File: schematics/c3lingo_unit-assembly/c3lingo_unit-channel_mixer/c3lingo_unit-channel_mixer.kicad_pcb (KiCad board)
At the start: 2 copper layers, 75 x 90 mm, 103 parts, among them J301 Interconnect, J303 I/O, Q301 MMBFJ113, SW301 OnAir_X, SW302 Mute_X, U301 TL072, U302 LM339, U303 LM339, U304 LM339, U305 LM833-N

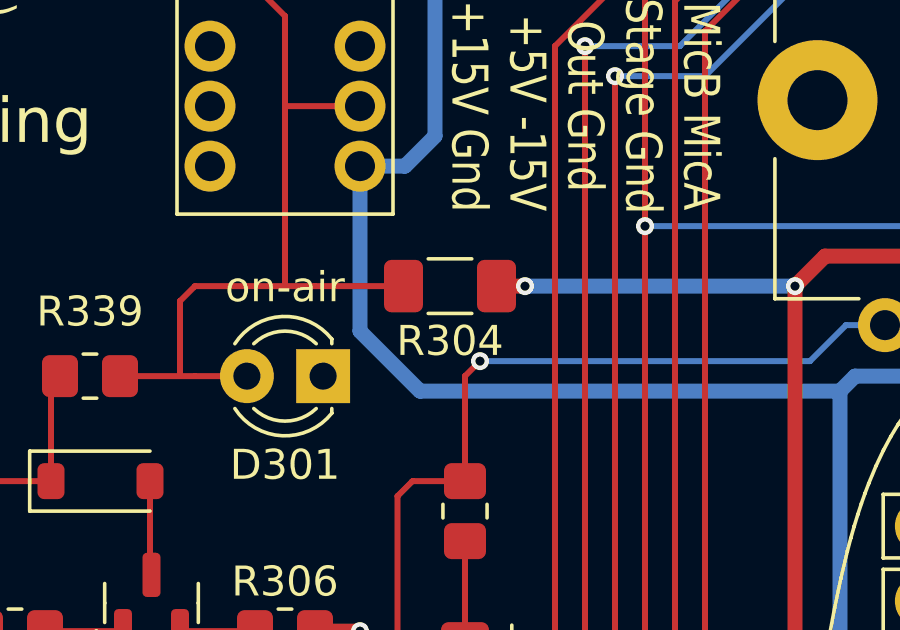
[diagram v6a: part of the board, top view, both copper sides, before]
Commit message: Channel-Mixer: Fix on-air LED resistor
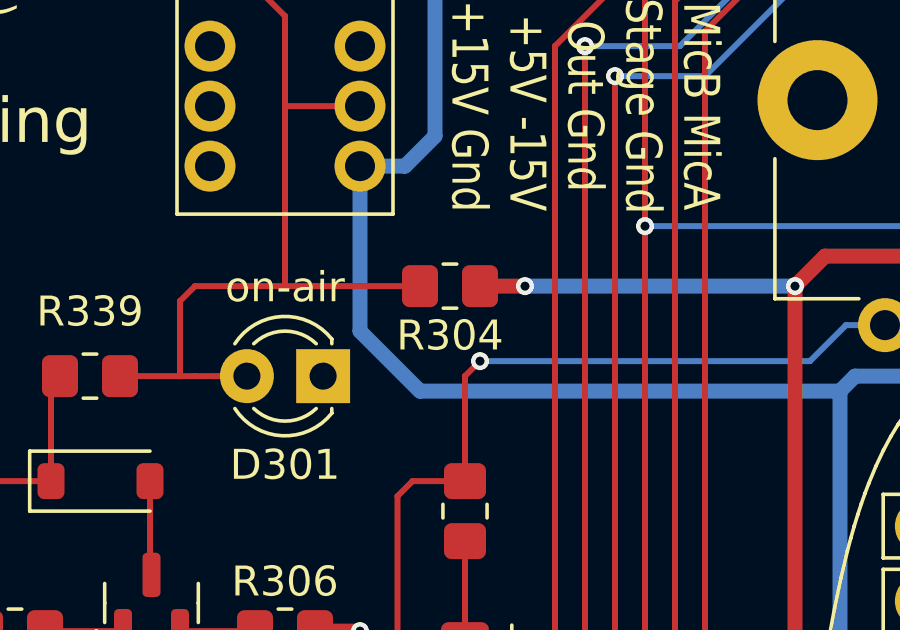
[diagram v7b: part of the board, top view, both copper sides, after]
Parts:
- R304: value 1K, 0.25W -> 3.3K; footprint Resistor_SMD:R_1206_3216Metric_Pad1.30x1.75mm_HandSolder -> Resistor_SMD:R_0805_2012Metric_Pad1.20x1.40mm_HandSolder
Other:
- board text added: "c3lingo Interpreter Unit Channel Mixer v1.0.1 2024-10-29"
- board text removed: "c3lingo Interpreter Unit Channel Mixer v1.0.0 2024-10-16"
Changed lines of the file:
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@@
 	(title_block
 		(title "c3lingo interpeter unit -- channel mixer")
-		(date "2025-10-16")
-		(rev "v1.0.0")
+		(date "2025-10-29")
+		(rev "v1.0.1")
 		(company "c3lingo/ c3voc: jtbx and collaborators")
 	)
@@
 		)
 	)
-	(footprint "Resistor_SMD:R_1206_3216Metric_Pad1.30x1.75mm_HandSolder"
+	(footprint "Resistor_SMD:R_0805_2012Metric_Pad1.20x1.40mm_HandSolder"
 		(layer "F.Cu")
 		(at 70.5 104 180)
-		(descr "Resistor SMD 1206 (3216 Metric), square (rectangular) end terminal, IPC-7351 nominal with elongated pad for handsoldering. (Body size source: IPC-SM-782 page 72, https://www.pcb-3d.com/wordpress/wp-content/uploads/ipc-sm-782a_amendment_1_and_2.pdf), generated with kicad-footprint-generator")
+		(descr "Resistor SMD 0805 (2012 Metric), square (rectangular) end terminal, IPC-7351 nominal with elongated pad for handsoldering. (Body size source: IPC-SM-782 page 72, https://www.pcb-3d.com/wordpress/wp-content/uploads/ipc-sm-782a_amendment_1_and_2.pdf), generated with kicad-footprint-generator")
 		(tags "resistor handsolder")
 		(property "Reference" "R304"
-			(at 0 -1.83 180)
+			(at 0 -1.65 180)
 			(layer "F.SilkS")
 			(effects
@@
 			)
 		)
-		(property "Value" "1K, 0.25W"
-			(at 0 1.83 180)
+		(property "Value" "3.3K"
+			(at 0 1.65 180)
 			(layer "F.Fab")
 			(effects
@@
 			)
 		)
-		(property "LCSC Part #" "C4410"
+		(property "LCSC Part #" "C26010"
 			(at 0 0 180)
 			(unlocked yes)
@@
 		(attr smd)
 		(fp_line
-			(start -0.727064 0.91)
-			(end 0.727064 0.91)
+			(start -0.227064 0.735)
+			(end 0.227064 0.735)
 			(stroke
 				(width 0.12)
@@
 		)
 		(fp_line
-			(start -0.727064 -0.91)
-			(end 0.727064 -0.91)
+			(start -0.227064 -0.735)
+			(end 0.227064 -0.735)
 			(stroke
 				(width 0.12)
@@
 		)
 		(fp_line
-			(start 2.45 1.13)
-			(end -2.45 1.13)
+			(start 1.85 0.95)
+			(end -1.85 0.95)
 			(stroke
 				(width 0.05)
@@
 		)
 		(fp_line
-			(start 2.45 -1.13)
-			(end 2.45 1.13)
+			(start 1.85 -0.95)
+			(end 1.85 0.95)
 			(stroke
 				(width 0.05)
@@
 		)
 		(fp_line
-			(start -2.45 1.13)
-			(end -2.45 -1.13)
+			(start -1.85 0.95)
+			(end -1.85 -0.95)
 			(stroke
 				(width 0.05)
@@
 		)
 		(fp_line
-			(start -2.45 -1.13)
-			(end 2.45 -1.13)
+			(start -1.85 -0.95)
+			(end 1.85 -0.95)
 			(stroke
 				(width 0.05)
@@
 		)
 		(fp_line
-			(start 1.6 0.8)
-			(end -1.6 0.8)
+			(start 1 0.625)
+			(end -1 0.625)
 			(stroke
 				(width 0.1)
@@
 		)
 		(fp_line
-			(start 1.6 -0.8)
-			(end 1.6 0.8)
+			(start 1 -0.625)
+			(end 1 0.625)
 			(stroke
 				(width 0.1)
@@
 		)
 		(fp_line
-			(start -1.6 0.8)
-			(end -1.6 -0.8)
+			(start -1 0.625)
+			(end -1 -0.625)
 			(stroke
 				(width 0.1)
@@
 		)
 		(fp_line
-			(start -1.6 -0.8)
-			(end 1.6 -0.8)
+			(start -1 -0.625)
+			(end 1 -0.625)
 			(stroke
 				(width 0.1)
@@
 			(effects
 				(font
-					(size 0.8 0.8)
-					(thickness 0.12)
+					(size 0.5 0.5)
+					(thickness 0.08)
 				)
 			)
 		)
 		(pad "1" smd roundrect
-			(at -1.55 0 180)
-			(size 1.3 1.75)
+			(at -1 0 180)
+			(size 1.2 1.4)
 			(layers "F.Cu" "F.Mask" "F.Paste")
-			(roundrect_rratio 0.192308)
+			(roundrect_rratio 0.208333)
 			(net 2 "+15V")
 			(pintype "passive")
 		)
 		(pad "2" smd roundrect
-			(at 1.55 0 180)
-			(size 1.3 1.75)
+			(at 1 0 180)
+			(size 1.2 1.4)
 			(layers "F.Cu" "F.Mask" "F.Paste")
-			(roundrect_rratio 0.192308)
+			(roundrect_rratio 0.208333)
 			(net 66 "Net-(D301-A)")
 			(pintype "passive")
 		)
 		(embedded_fonts no)
-		(model "${KICAD9_3DMODEL_DIR}/Resistor_SMD.3dshapes/R_1206_3216Metric.step"
+		(model "${KICAD9_3DMODEL_DIR}/Resistor_SMD.3dshapes/R_0805_2012Metric.step"
 			(offset
 				(xyz 0 0 0)
@@
 		)
 	)
-	(gr_text "c3lingo Interpreter Unit\nChannel Mixer\nv1.0.0 2024-10-16"
+	(gr_text "c3lingo Interpreter Unit\nChannel Mixer\nv1.0.1 2024-10-29"
 		(at 87.5 87.5 0)
 		(layer "B.SilkS")
